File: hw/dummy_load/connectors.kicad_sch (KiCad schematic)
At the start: 35 parts, among them J1 12V optional, J10 Calib gain, J11 Calib divider, J12 12V in, J13 Conn_01x20, J14 Conn_01x20, J2 NTC DUT, J3 NTC Ambient, J4 NTC Heatsink, J5 Fan1, J6 Fan2, J7 NTC Heatsink, J8 NTC Heatsink, J9 NTC Heatsink, Q1 DMN2056U, U4 PHOENIX_1017503

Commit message: Replace terminal block, update BOM and datasheets, minor fixes to tracing
Signed-off-by: Mateusz Pajak <22417805+Tai-Min@users.noreply.github.com>
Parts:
- removed U4: PHOENIX_1017503, Library:PHOENIX_1017503, symbol Phoenix:1017503
- added X1: WAGO 2604-1102, Library:WAGO-2604-1102, symbol WAGO:WAGO 2604-1102
- J13, J14: LCSC Part # TODO: -> C18078139
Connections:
- net GND: now also X1.P1.1, X1.P1.2
- net at F3.2: now also X1.P2.1, X1.P2.2
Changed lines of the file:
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@@
 			)
 		)
-		(property "Datasheet" "TODO:"
+		(property "Datasheet" "\".\\datasheets\\PicoHeaders.pdf\""
 			(at 86.36 163.83 0)
 			(effects
@@
 			)
 		)
-		(property "LCSC Part #" "TODO:"
+		(property "LCSC Part #" "C18078139"
 			(at 86.36 163.83 90)
 			(effects
@@
 				(path "/12389ac2-8de8-4a31-87e8-c4842210736c/a7cbcb5a-a6ff-4407-a00f-1dbbab846046"
 					(reference "D4")
+					(unit 1)
+				)
+			)
+		)
+	)
+	(symbol
+		(lib_id "WAGO:WAGO 2604-1102")
+		(at 231.14 132.08 0)
+		(mirror x)
+		(unit 1)
+		(exclude_from_sim no)
+		(in_bom yes)
+		(on_board yes)
+		(dnp no)
+		(property "Reference" "X1"
+			(at 231.394 136.906 0)
+			(effects
+				(font
+					(size 1.27 1.27)
+				)
+				(justify left bottom)
+				(hide yes)
+			)
+		)
+		(property "Value" "WAGO 2604-1102"
+			(at 236.474 133.858 0)
+			(effects
+				(font
+					(size 1.27 1.27)
+				)
+			)
+		)
+		(property "Footprint" "Library:WAGO-2604-1102"
+			(at 252.222 132.08 0)
+			(effects
+				(font
+					(size 1.27 1.27)
+				)
+				(justify bottom)
+				(hide yes)
+			)
+		)
+		(property "Datasheet" "\".\\datasheets\\WAGO_2604-1102.pdf\""
+			(at 231.14 132.08 0)
+			(effects
+				(font
+					(size 1.27 1.27)
+				)
+				(hide yes)
+			)
+		)
+		(property "Description" ""
+			(at 231.14 132.08 0)
+			(effects
+				(font
+					(size 1.27 1.27)
+				)
+				(hide yes)
+			)
+		)
+		(property "LCSC Part #" "https://www.tme.eu/us/en-us/details/2604-1102/listwy-zaciskowe-do-druku/wago/"
+			(at 231.14 132.08 0)
+			(effects
+				(font
+					(size 1.27 1.27)
+				)
+				(hide yes)
+			)
+		)
+		(pin "P2.2"
+		)
+		(pin "P2.1"
+		)
+		(pin "P1.2"
+		)
+		(pin "P1.1"
+		)
+		(instances
+			(project ""
+				(path "/12389ac2-8de8-4a31-87e8-c4842210736c/a7cbcb5a-a6ff-4407-a00f-1dbbab846046"
+					(reference "X1")
 					(unit 1)
 				)
@@
 			)
 		)
-		(property "Datasheet" "TODO:"
+		(property "Datasheet" "\".\\datasheets\\PicoHeaders.pdf\""
 			(at 86.36 179.07 0)
 			(effects
@@
 			)
 		)
-		(property "LCSC Part #" "TODO:"
+		(property "LCSC Part #" "C18078139"
 			(at 86.36 179.07 90)
 			(effects
@@
 					(unit 1)
 				)
-			)
-		)
-	)
-	(symbol
-		(lib_id "Phoenix:1017503")
-		(at 236.22 119.38 0)
-		(unit 1)
-		(exclude_from_sim no)
-		(in_bom yes)
-		(on_board yes)
-		(dnp no)
-		(property "Reference" "U4"
-			(at 230.632 117.094 0)
-			(effects
-				(font
-					(size 1.27 1.27)
-				)
-				(justify left)
-			)
-		)
-		(property "Value" "PHOENIX_1017503"
-			(at 230.632 119.634 0)
-			(effects
-				(font
-					(size 1.27 1.27)
-				)
-				(justify left)
-			)
-		)
-		(property "Footprint" "Library:PHOENIX_1017503"
-			(at 236.22 119.38 0)
-			(effects
-				(font
-					(size 1.27 1.27)
-				)
-				(hide yes)
-			)
-		)
-		(property "Datasheet" "\".\\datasheets\\PHOENIX_1017503.pdf\""
-			(at 236.22 119.38 0)
-			(effects
-				(font
-					(size 1.27 1.27)
-				)
-				(hide yes)
-			)
-		)
-		(property "Description" ""
-			(at 236.22 119.38 0)
-			(effects
-				(font
-					(size 1.27 1.27)
-				)
-				(hide yes)
-			)
-		)
-		(property "LCSC Part #" "~"
-			(at 236.22 119.38 0)
-			(effects
-				(font
-					(size 1.27 1.27)
-				)
-				(hide yes)
-			)
-		)
-		(pin "1_1"
-		)
-		(pin "1_2"
-		)
-		(pin "2_1"
-		)
-		(pin "2_2"
-		)
-		(instances
-			(project "dummy_load"
-				(path "/12389ac2-8de8-4a31-87e8-c4842210736c/a7cbcb5a-a6ff-4407-a00f-1dbbab846046"
-					(reference "U4")
-					(unit 1)
-				)

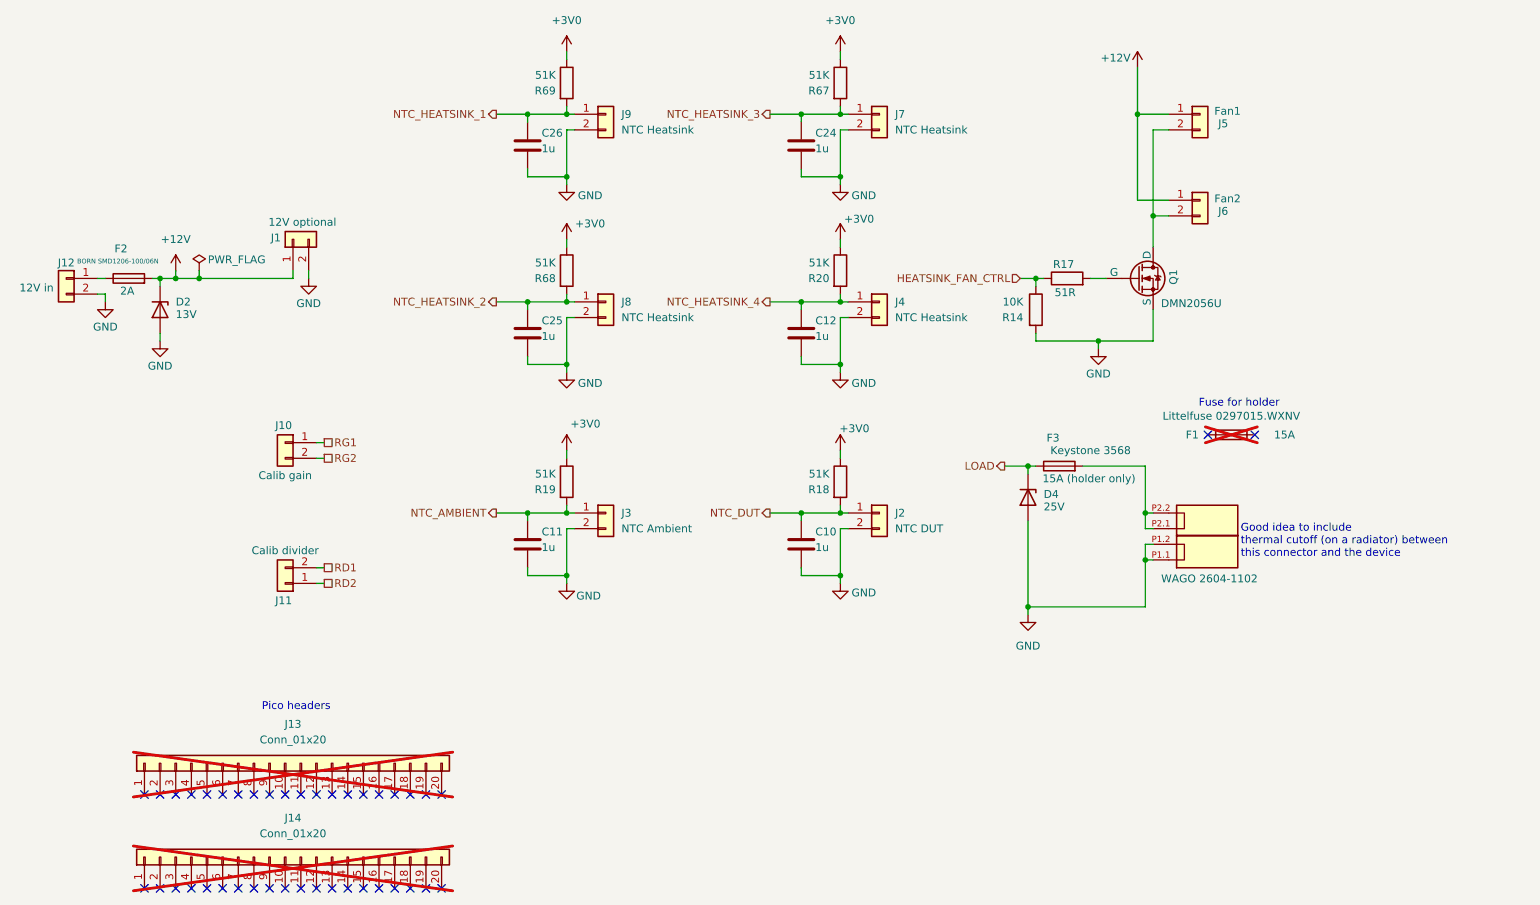
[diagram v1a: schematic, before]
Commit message: Better PCB design, update BOM, add UART header for debugging (#7)
Signed-off-by: Mateusz Pajak <22417805+Tai-Min@users.noreply.github.com>
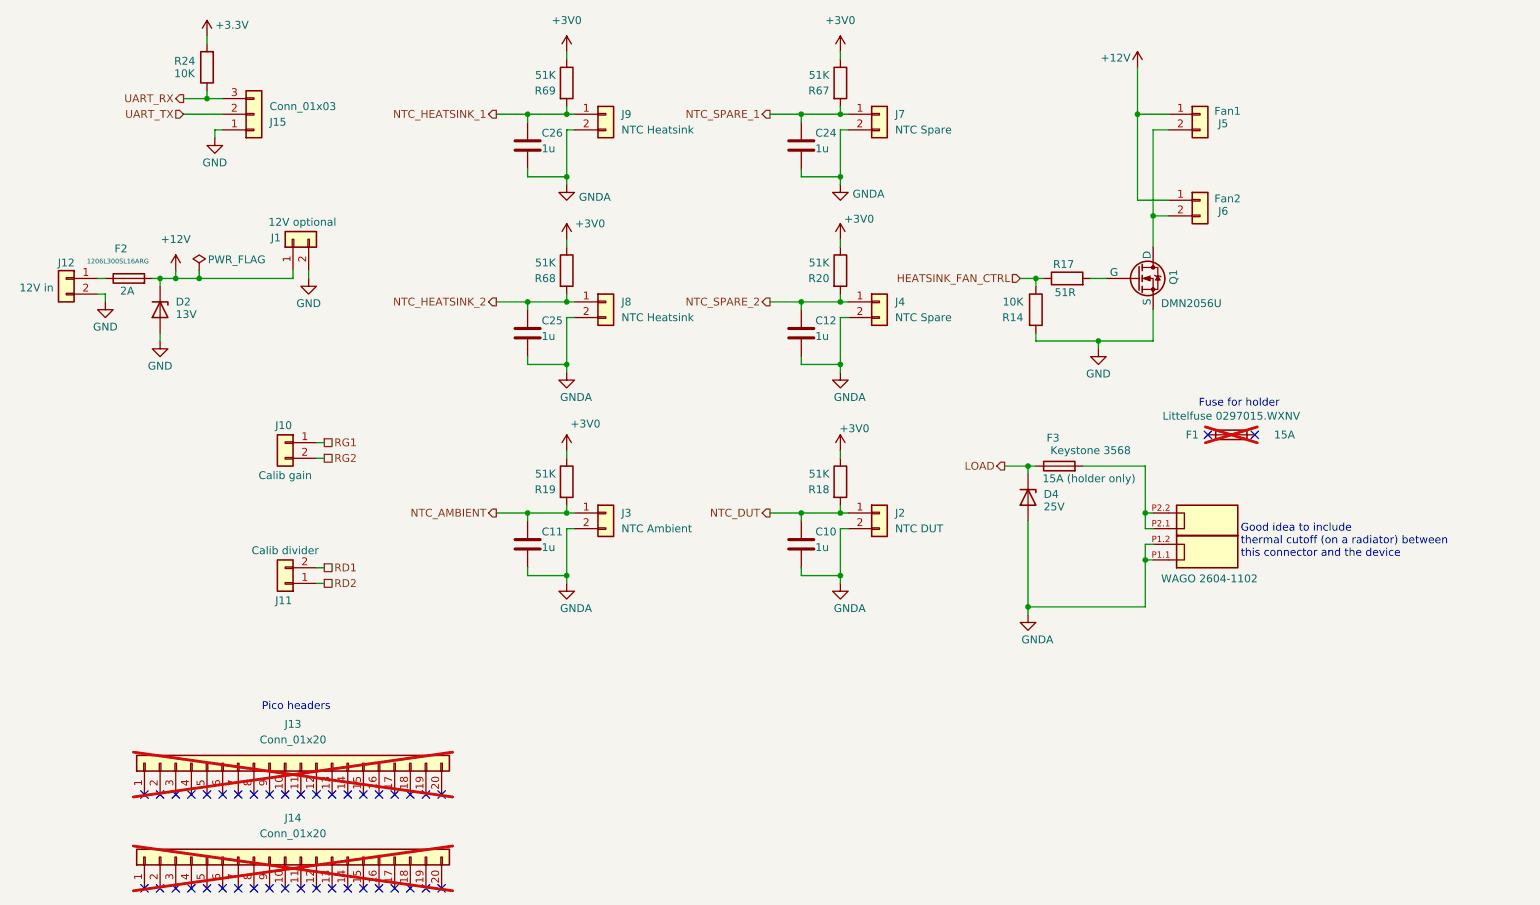
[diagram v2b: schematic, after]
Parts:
- added J15: Conn_01x03, Connector_JST:JST_XH_B3B-XH-A_1x03_P2.50mm_Vertical, symbol Connector_Generic:Conn_01x03
- added R24: 10K, Resistor_SMD:R_0603_1608Metric, symbol Device:R
- C10, C11, C12, C24, C25, C26: footprint Capacitor_SMD:C_1206_3216Metric_Pad1.33x1.80mm_HandSolder -> Capacitor_SMD:C_0603_1608Metric; LCSC Part # C1848 -> C15849
- F2: value BORN SMD1206-100/06N -> 1206L300SL16ARG; footprint Fuse:Fuse_1206_3216Metric_Pad1.42x1.75mm_HandSolder -> Fuse:Fuse_1206_3216Metric; LCSC Part # C6165191 -> C28326707
- J4, J7: value NTC Heatsink -> NTC Spare
- Q1: footprint Package_TO_SOT_SMD:TSOT-23_HandSoldering -> Package_TO_SOT_SMD:TSOT-23
- R14: footprint Resistor_SMD:R_1206_3216Metric_Pad1.30x1.75mm_HandSolder -> Resistor_SMD:R_0603_1608Metric; LCSC Part # C17902 -> C98220
- R17: footprint Resistor_SMD:R_1206_3216Metric_Pad1.30x1.75mm_HandSolder -> Resistor_SMD:R_0603_1608Metric; LCSC Part # C2907517 -> C2907181
- R18, R19, R20, R67, R68, R69: footprint Resistor_SMD:R_1206_3216Metric_Pad1.30x1.75mm_HandSolder -> Resistor_SMD:R_0603_1608Metric; LCSC Part # C2933722 -> C107231
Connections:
- net GND: now also J15.1 (Pin_1); no longer C10.1, C11.1, C12.1, C24.1, C25.1, C26.1, D4.2 (A), J2.2 (Pin_2), J3.2 (Pin_2), J4.2 (Pin_2), J7.2 (Pin_2), J8.2 (Pin_2), J9.2 (Pin_2), X1.P1.1, X1.P1.2
- net NTC_HEATSINK_3 renamed NTC_SPARE_1
- net NTC_HEATSINK_4 renamed NTC_SPARE_2
- new net +3.3V: R24.2
- new net GNDA: C10.1, C11.1, C12.1, C24.1, C25.1, C26.1, D4.2 (A), J2.2 (Pin_2), J3.2 (Pin_2), J4.2 (Pin_2), J7.2 (Pin_2), J8.2 (Pin_2), J9.2 (Pin_2), X1.P1.1, X1.P1.2
- new net UART_RX: J15.3 (Pin_3), R24.1
- new net UART_TX: J15.2 (Pin_2)
